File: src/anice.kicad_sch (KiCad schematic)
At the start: 7 parts, among them J1 Conn_02x20_Counter_Clockwise, U1 ECP5U_12_CABGA256

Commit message: Rev 2
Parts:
- C43: LCSC Part (none) -> C1525
- J1: now not fitted
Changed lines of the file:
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@@
 			)
 		)
-		(property "LCSC Part" ""
+		(property "LCSC Part" "C1525"
 			(at 151.13 27.94 0)
 			(effects
@@
 		(in_bom yes)
 		(on_board yes)
-		(dnp no)
+		(dnp yes)
 		(fields_autoplaced yes)
 		(property "Reference" "J1"

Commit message: Tidy project
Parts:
- C43: JLCPCB Part # (none) -> C1525; LCSC Part C1525 -> (none)
- U1: JLCPCB Part # (none) -> C1521614; LCSC Part C1521614 -> (none)
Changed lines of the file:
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@@
 			)
 		)
-		(property "LCSC Part" "C1525"
+		(property "JLCPCB Part #" "C1525"
 			(at 151.13 27.94 0)
 			(effects
@@
 					(size 1.27 1.27)
 				)
-				(hide yes)
 			)
 		)
@@
 			)
 		)
-		(property "LCSC Part" ""
-			(at 252.73 147.32 0)
-			(effects
-				(font
-					(size 1.27 1.27)
-				)
-				(hide yes)
-			)
-		)
 		(instances
 			(project "anice"
@@
 		)
 		(property "Description" "Generic connector, double row, 02x20, odd/even pin numbering scheme (row 1 odd numbers, row 2 even numbers), script generated (kicad-library-utils/schlib/autogen/connector/)"
-			(at 195.58 60.96 0)
-			(effects
-				(font
-					(size 1.27 1.27)
-				)
-				(hide yes)
-			)
-		)
-		(property "LCSC Part" ""
 			(at 195.58 60.96 0)
 			(effects
@@
 			)
 		)
-		(property "LCSC Part" " C1521614"
+		(property "JLCPCB Part #" " C1521614"
 			(at 116.84 71.12 0)
 			(effects
@@
 					(size 1.27 1.27)
 				)
-				(hide yes)
-			)
-		)
+			)
+		)

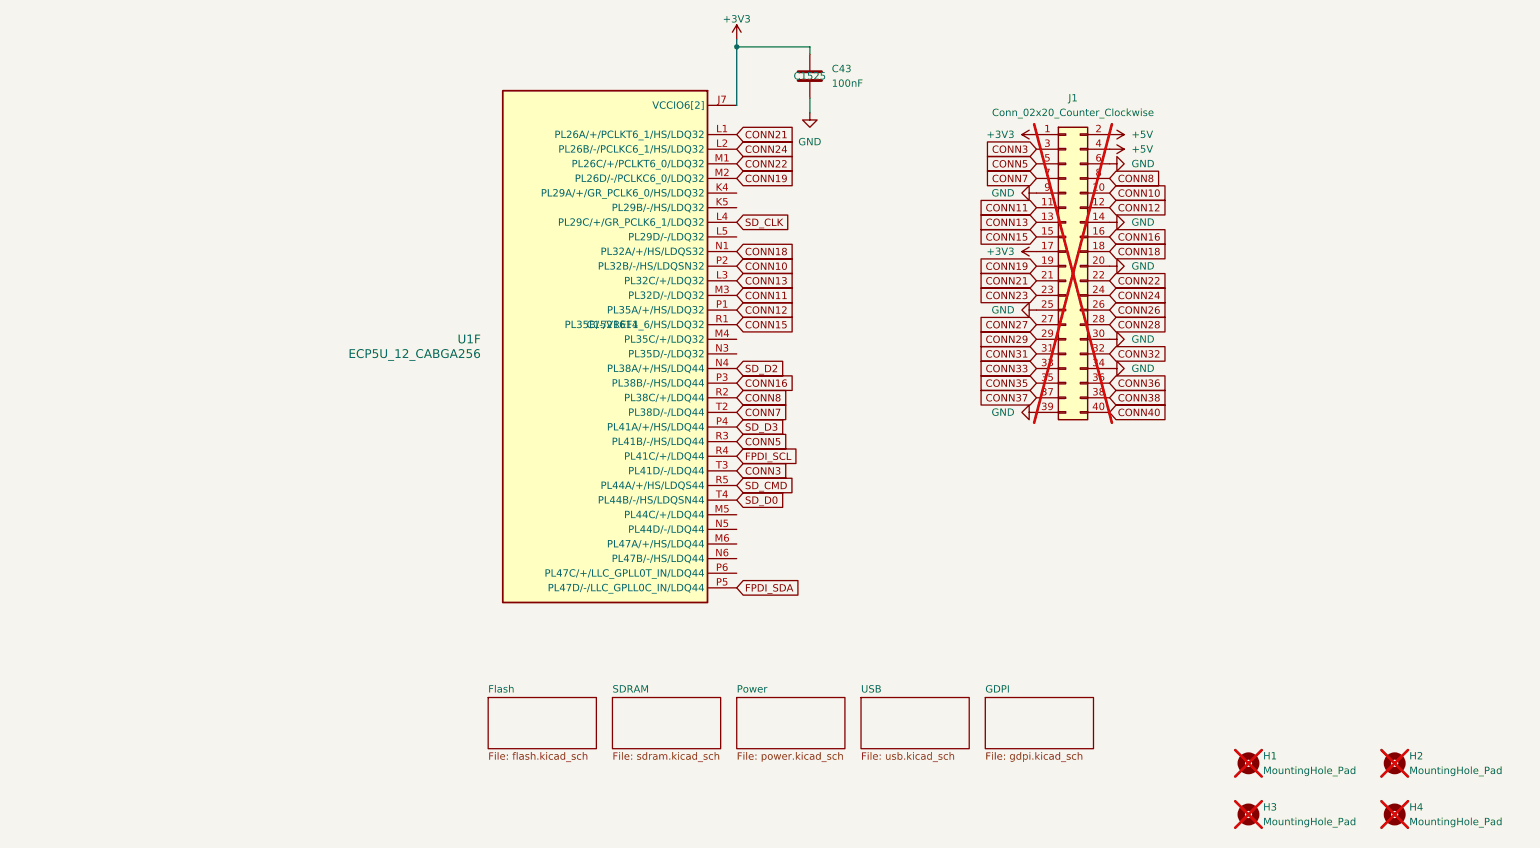
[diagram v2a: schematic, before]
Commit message: Add test points
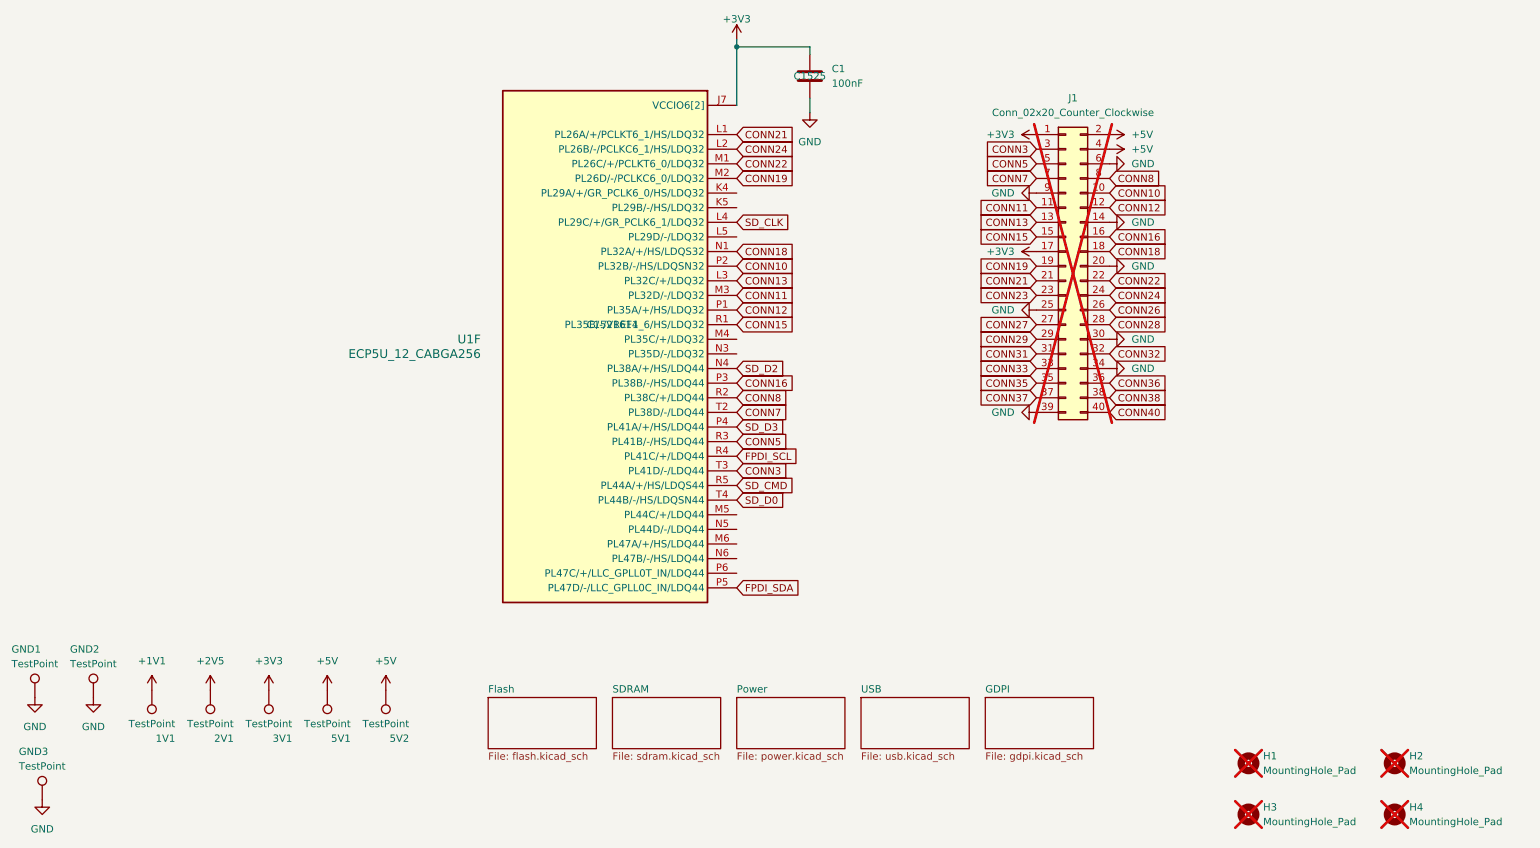
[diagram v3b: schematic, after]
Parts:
- added 1V1, 2V1, 3V1, 5V1, 5V2, GND1, GND2, GND3: TestPoint, TestPoint:TestPoint_Pad_D1.5mm, symbol Connector:TestPoint
- renumbered C43 to C1
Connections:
- net +3V3: now also 3V1.1
- net +5V: now also 5V1.1, 5V2.1
- net GND: now also GND1.1, GND2.1, GND3.1
- new net +1V1: 1V1.1
- new net +2V5: 2V1.1
